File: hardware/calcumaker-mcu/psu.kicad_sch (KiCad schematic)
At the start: 21 parts, among them J1 USB-C, J2 BAT 1S Li-ion, Q1 AO3401A, U2 TPS63900DSKR, U3 USBLC6-2SC6, U4 MCP73831-2-OT

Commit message: hardware: 3-board split (MCU + keyboard + display), wired display, real connectors
Split the single logic board into three, wire the display as a KiCad
multi-channel design, and settle every interconnect on real, in-stock parts.

Three-board split (was two):
- Rename calcumaker-main -> calcumaker-mcu (brain/PSU logic board).
- New calcumaker-keyboard board: 50-key Cherry MX matrix + its own
  STM32G031K8U6 scanner (LCSC C432207, UFQFPN-32) + annunciator LEDs,
  mezzanine-stacked above the MCU board. Keyscanning is off the main board;
  only an I2C + UART link + KB_IRQ wake + power cross the mezzanine.

Display board (calcumaker-display):
- Corrected FJ5161AH to a SINGLE-digit 0.56" common-cathode part (C8093) --
  it is NOT a 4-digit module; 48 single digits (16/row x 3), authored symbol
  + 0.56" LTS6760 land. The old 4-digit CC56-12 mapping (and its 3D model)
  was the phantom "clock colon".
- Rebuilt as a KiCad multi-channel design: one reusable display_row.kicad_sch
  (1 TM1640 + 16 digits, fully wired) instantiated x3. Extended kschgen.py
  with wiring primitives + reused-sheet (multi-channel) support.

Connectors (real, verified LCSC / DigiKey parts):
- Display link -> 0.5mm 12P FFC: AFC01-S12FCA-00 (LCSC C262661) on both
  boards; cable = GCT FFC05-TIN 05-12-A-<len>-A-4-06-4-T (DigiKey accessory,
  length TBD). +5V/GND conductors doubled for the display LED current.
- Keyboard mezzanine -> low-profile Hirose DF40 (0.4mm, 2x5, 1.5mm stack):
  DF40C-10DS (C424636) + DF40C-10DP (C424635) -- dedicated KiCad footprint
  + 3D model, unlike the datasheet-less generic parts first considered.

Low-power & wake documented (two Stop domains; keypress -> G0 EXTI wake ->
KB_IRQ -> U575 WKUP; G0 also wakes on I2C address-match). calcumaker-core
is unchanged -- App still consumes (row,col).

All three boards generate + pass the structure check (mcu 52 / keyboard 119 /
display 60 components, all footprints assigned, no duplicate refs). Docs
(DESIGN.md, PARTS.md incl. a Non-B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
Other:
- title: Calcumaker 16 — Main — USB-C / Li-ion charge / load-share / buck-boost -> Calcumaker 16 — MCU — USB-C / Li-ion charge / load-share / buck-boost
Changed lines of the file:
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@@
 	(paper "A3")
 	(title_block
-		(title "Calcumaker 16 — Main — USB-C / Li-ion charge / load-share / buck-boost")
-		(date "2026-06-21")
-		(rev "0.1")
+		(title "Calcumaker 16 — MCU — USB-C / Li-ion charge / load-share / buck-boost")
+		(date "2026-07-05")
+		(rev "0.2")
 		(company "calcumaker authors")
 	)
@@
 		(pin "SH")
 		(instances
-			(project "calcumaker-main"
-				(path "/ca1c0000-0000-4000-8000-00000000ma01/b9ee67a8-aaed-4504-a49b-ae68f7f164a3"
+			(project "calcumaker-mcu"
+				(path "/ca1c0000-0000-4000-8000-00000000ma01/672f4fa7-1cc1-4703-8edf-f066cdb44902"
 					(reference "J1")
 					(unit 1)
@@
 		(pin "2")
 		(instances
-			(project "calcumaker-main"
-				(path "/ca1c0000-0000-4000-8000-00000000ma01/b9ee67a8-aaed-4504-a49b-ae68f7f164a3"
+			(project "calcumaker-mcu"
+				(path "/ca1c0000-0000-4000-8000-00000000ma01/672f4fa7-1cc1-4703-8edf-f066cdb44902"
 					(reference "J2")
 					(unit 1)
@@
 		(pin "11")
 		(instances
-			(project "calcumaker-main"
-				(path "/ca1c0000-0000-4000-8000-00000000ma01/b9ee67a8-aaed-4504-a49b-ae68f7f164a3"
+			(project "calcumaker-mcu"
+				(path "/ca1c0000-0000-4000-8000-00000000ma01/672f4fa7-1cc1-4703-8edf-f066cdb44902"
 					(reference "U2")
 					(unit 1)
@@
 		(pin "6")
 		(instances
-			(project "calcumaker-main"
-				(path "/ca1c0000-0000-4000-8000-00000000ma01/b9ee67a8-aaed-4504-a49b-ae68f7f164a3"
+			(project "calcumaker-mcu"
+				(path "/ca1c0000-0000-4000-8000-00000000ma01/672f4fa7-1cc1-4703-8edf-f066cdb44902"
 					(reference "U3")
 					(unit 1)
@@
 		(pin "2")
 		(instances
-			(project "calcumaker-main"
-				(path "/ca1c0000-0000-4000-8000-00000000ma01/b9ee67a8-aaed-4504-a49b-ae68f7f164a3"
+			(project "calcumaker-mcu"
+				(path "/ca1c0000-0000-4000-8000-00000000ma01/672f4fa7-1cc1-4703-8edf-f066cdb44902"
 					(reference "R1")
 					(unit 1)
@@
 		(pin "2")
 		(instances
-			(project "calcumaker-main"
-				(path "/ca1c0000-0000-4000-8000-00000000ma01/b9ee67a8-aaed-4504-a49b-ae68f7f164a3"
+			(project "calcumaker-mcu"
+				(path "/ca1c0000-0000-4000-8000-00000000ma01/672f4fa7-1cc1-4703-8edf-f066cdb44902"
 					(reference "R2")
 					(unit 1)
@@
 		(pin "5")
 		(instances
-			(project "calcumaker-main"
-				(path "/ca1c0000-0000-4000-8000-00000000ma01/b9ee67a8-aaed-4504-a49b-ae68f7f164a3"
+			(project "calcumaker-mcu"
+				(path "/ca1c0000-0000-4000-8000-00000000ma01/672f4fa7-1cc1-4703-8edf-f066cdb44902"
 					(reference "U4")
 					(unit 1)
@@
 		(pin "2")
 		(instances
-			(project "calcumaker-main"
-				(path "/ca1c0000-0000-4000-8000-00000000ma01/b9ee67a8-aaed-4504-a49b-ae68f7f164a3"
+			(project "calcumaker-mcu"
+				(path "/ca1c0000-0000-4000-8000-00000000ma01/672f4fa7-1cc1-4703-8edf-f066cdb44902"
 					(reference "R3")
 					(unit 1)
@@
 		(pin "2")
 		(instances
-			(project "calcumaker-main"
-				(path "/ca1c0000-0000-4000-8000-00000000ma01/b9ee67a8-aaed-4504-a49b-ae68f7f164a3"
+			(project "calcumaker-mcu"
+				(path "/ca1c0000-0000-4000-8000-00000000ma01/672f4fa7-1cc1-4703-8edf-f066cdb44902"
 					(reference "C1")
 					(unit 1)
@@
 		(pin "2")
 		(instances
-			(project "calcumaker-main"
-				(path "/ca1c0000-0000-4000-8000-00000000ma01/b9ee67a8-aaed-4504-a49b-ae68f7f164a3"
+			(project "calcumaker-mcu"
+				(path "/ca1c0000-0000-4000-8000-00000000ma01/672f4fa7-1cc1-4703-8edf-f066cdb44902"
 					(reference "C2")
 					(unit 1)
@@
 		(pin "3")
 		(instances
-			(project "calcumaker-main"
-				(path "/ca1c0000-0000-4000-8000-00000000ma01/b9ee67a8-aaed-4504-a49b-ae68f7f164a3"
+			(project "calcumaker-mcu"
+				(path "/ca1c0000-0000-4000-8000-00000000ma01/672f4fa7-1cc1-4703-8edf-f066cdb44902"
 					(reference "Q1")
 					(unit 1)
@@
 		(pin "2")
 		(instances
-			(project "calcumaker-main"
-				(path "/ca1c0000-0000-4000-8000-00000000ma01/b9ee67a8-aaed-4504-a49b-ae68f7f164a3"
+			(project "calcumaker-mcu"
+				(path "/ca1c0000-0000-4000-8000-00000000ma01/672f4fa7-1cc1-4703-8edf-f066cdb44902"
 					(reference "D1")
 					(unit 1)
@@
 		(pin "2")
 		(instances
-			(project "calcumaker-main"
-				(path "/ca1c0000-0000-4000-8000-00000000ma01/b9ee67a8-aaed-4504-a49b-ae68f7f164a3"
+			(project "calcumaker-mcu"
+				(path "/ca1c0000-0000-4000-8000-00000000ma01/672f4fa7-1cc1-4703-8edf-f066cdb44902"
 					(reference "R4")
 					(unit 1)
@@
 		(pin "2")
 		(instances
-			(project "calcumaker-main"
-				(path "/ca1c0000-0000-4000-8000-00000000ma01/b9ee67a8-aaed-4504-a49b-ae68f7f164a3"
+			(project "calcumaker-mcu"
+				(path "/ca1c0000-0000-4000-8000-00000000ma01/672f4fa7-1cc1-4703-8edf-f066cdb44902"
 					(reference "L1")
 					(unit 1)
@@
 		(pin "2")
 		(instances
-			(project "calcumaker-main"
-				(path "/ca1c0000-0000-4000-8000-00000000ma01/b9ee67a8-aaed-4504-a49b-ae68f7f164a3"
+			(project "calcumaker-mcu"
+				(path "/ca1c0000-0000-4000-8000-00000000ma01/672f4fa7-1cc1-4703-8edf-f066cdb44902"
 					(reference "C3")
 					(unit 1)
@@
 		(pin "2")
 		(instances
-			(project "calcumaker-main"
-				(path "/ca1c0000-0000-4000-8000-00000000ma01/b9ee67a8-aaed-4504-a49b-ae68f7f164a3"
+			(project "calcumaker-mcu"
+				(path "/ca1c0000-0000-4000-8000-00000000ma01/672f4fa7-1cc1-4703-8edf-f066cdb44902"
 					(reference "C4")
 					(unit 1)
@@
 		(pin "2")
 		(instances
-			(project "calcumaker-main"
-				(path "/ca1c0000-0000-4000-8000-00000000ma01/b9ee67a8-aaed-4504-a49b-ae68f7f164a3"
+			(project "calcumaker-mcu"
+				(path "/ca1c0000-0000-4000-8000-00000000ma01/672f4fa7-1cc1-4703-8edf-f066cdb44902"
 					(reference "C5")
 					(unit 1)
@@
 		(pin "2")
 		(instances
-			(project "calcumaker-main"
-				(path "/ca1c0000-0000-4000-8000-00000000ma01/b9ee67a8-aaed-4504-a49b-ae68f7f164a3"
+			(project "calcumaker-mcu"
+				(path "/ca1c0000-0000-4000-8000-00000000ma01/672f4fa7-1cc1-4703-8edf-f066cdb44902"
 					(reference "C6")
 					(unit 1)
@@
 		(pin "2")
 		(instances
-			(project "calcumaker-main"
-				(path "/ca1c0000-0000-4000-8000-00000000ma01/b9ee67a8-aaed-4504-a49b-ae68f7f164a3"
+			(project "calcumaker-mcu"
+				(path "/ca1c0000-0000-4000-8000-00000000ma01/672f4fa7-1cc1-4703-8edf-f066cdb44902"
 					(reference "C7")
 					(unit 1)
@@
 		(pin "2")
 		(instances
-			(project "calcumaker-main"
-				(path "/ca1c0000-0000-4000-8000-00000000ma01/b9ee67a8-aaed-4504-a49b-ae68f7f164a3"
+			(project "calcumaker-mcu"
+				(path "/ca1c0000-0000-4000-8000-00000000ma01/672f4fa7-1cc1-4703-8edf-f066cdb44902"
 					(reference "D2")
 					(unit 1)
@@
 		(pin "2")
 		(instances
-			(project "calcumaker-main"
-				(path "/ca1c0000-0000-4000-8000-00000000ma01/b9ee67a8-aaed-4504-a49b-ae68f7f164a3"
+			(project "calcumaker-mcu"
+				(path "/ca1c0000-0000-4000-8000-00000000ma01/672f4fa7-1cc1-4703-8edf-f066cdb44902"
 					(reference "R5")
 					(unit 1)

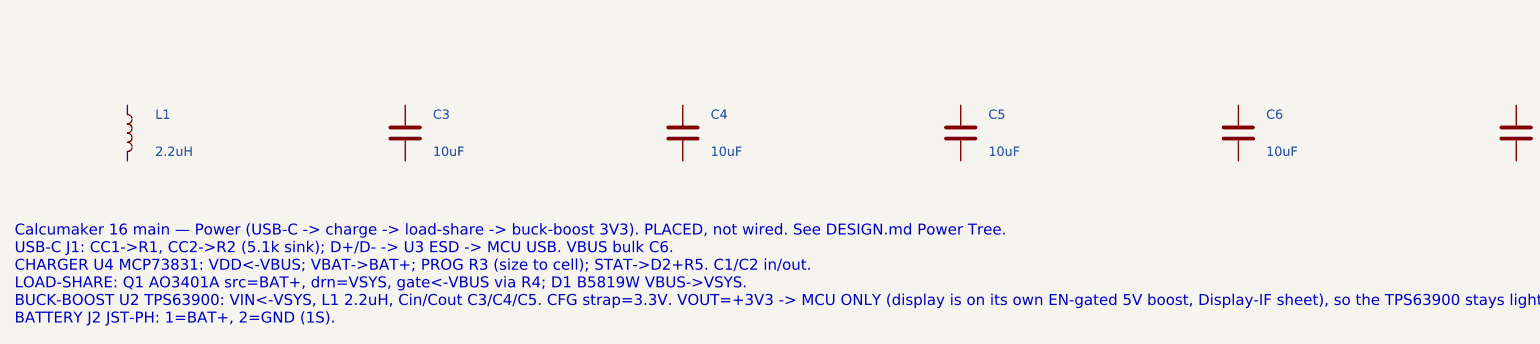
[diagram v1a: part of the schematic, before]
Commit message: docs: accuracy cleanup across README/DESIGN/PARTS + firmware/schgen comments
Sweep the docs and code comments to the three-board reality. Reviewed for
accuracy against the schematics/parts — no factual fixes were needed; this
also corrected several stale spots left over from the split:

- README / DESIGN.md / PARTS.md / reference: three-board split, 0.5mm FFC
  display link, Hirose DF40 mezzanine, STM32G0 keyboard scanner; drop stale
  "main board" phrasing; populate reference/README.md's datasheet table with
  the real parts (STM32G031K8U6, TM1640, FJ5161AH, AFC01-S12FCA-00 + GCT FFC,
  DF40C-10DS/DP).
- DESIGN.md Annunciators corrected to the keyboard board (D51-55 / R1-5,
  driven by the keyboard G0); Open Questions renumbered sequentially.
- firmware comments (keypad.rs / main.rs / Cargo.toml / README): keyboard-event
  intake over the mezzanine link + wake on KB_IRQ; fixed the wrong "host-tested
  with rug" note (it is the gmp-mpfr-nostd FFI). Comment-only, no logic change.
- schgen + .kicad_sch notes: "main" -> "MCU board", FFC/mezzanine references,
  TPS61022/MCU "no custom symbol".

All three boards still pass the structure check (mcu 52 / keyboard 119 /
display 60 components, no duplicate refs); the generator still compiles.

Co-Authored-By: Claude Opus 4.8 (1M context) <noreply@anthropic.com>
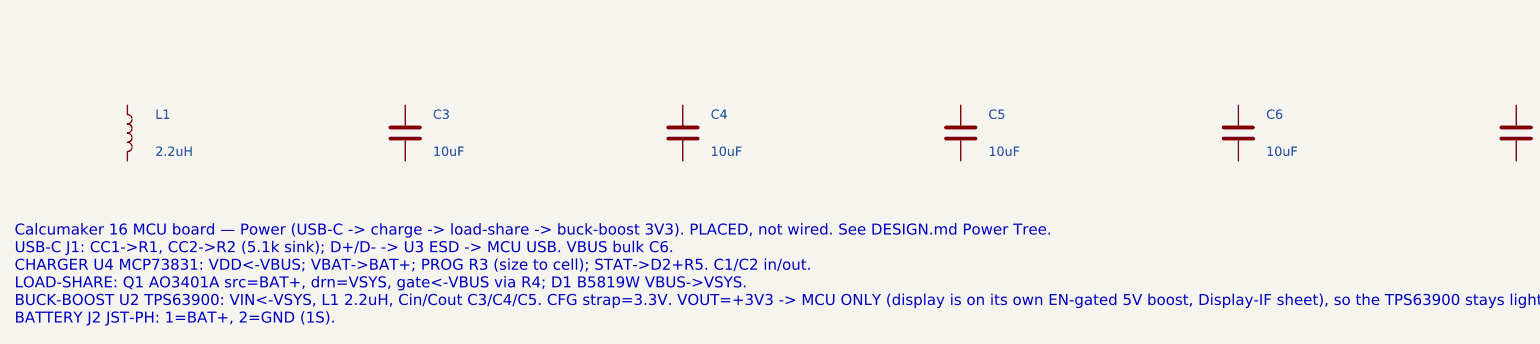
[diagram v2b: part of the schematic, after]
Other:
- note added: "Calcumaker 16 MCU board — Power (USB-C -> charge -> load-share -> buck-boost 3V3). PLACED, not wired. See DESIGN.md Power Tree. USB-C J1: CC1->R1, CC2->R2 (5.1k sink); D+/D- -> U3 ESD -> MCU USB. VBUS bulk C6. CHARGER U4 MCP73831: VDD<-VBUS; VBAT->BAT+; PROG R3 (size to cell); STAT->D2+R5. C1/C2 in/out. LOAD-SHARE: Q1 AO3401A src=BAT+, drn=VSYS, gate<-VBUS via R4; D1 B5819W VBUS->VSYS. BUCK-BOOST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"
- note removed: "Calcumaker 16 main — Power (USB-C -> charge -> load-share -> buck-boost 3V3). PLACED, not wired. See DESIGN.md Power Tree. USB-C J1: CC1->R1, CC2->R2 (5.1k sink); D+/D- -> U3 ESD -> MCU USB. VBUS bulk C6. CHARGER U4 MCP73831: VDD<-VBUS; VBAT->BAT+; PROG R3 (size to cell); STAT->D2+R5. C1/C2 in/out. LOAD-SHARE: Q1 AO3401A src=BAT+, drn=VSYS, gate<-VBUS via R4; D1 B5819W VBUS->VSYS. BUCK-BOOST U2 T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"
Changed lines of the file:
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@@
 		)
 	)
-	(text "Calcumaker 16 main — Power (USB-C -> charge -> load-share -> buck-boost 3V3). PLACED, not wired. See DESIGN.md Power Tree.\nUSB-C J1: CC1->R1, CC2->R2 (5.1k sink); D+/D- -> U3 ESD -> MCU USB. VBUS bulk C6.\nCHARGER U4 MCP73831: VDD<-VBUS; VBAT->BAT+; PROG R3 (size to cell); STAT->D2+R5. C1/C2 in/out.\nLOAD-SHARE: Q1 AO3401A src=BAT+, drn=VSYS, gate<-VBUS via R4; D1 B5819W VBUS->VSYS.\nBUCK-BOOST U2 TPS63900: VIN<-VSYS, L1 2.2uH, Cin/Cout C3/C4/C5. CFG strap=3.3V. VOUT=+3V3 -> MCU ONLY (display is on its own EN-gated 5V boost, Display-IF sheet), so the TPS63900 stays lightly loaded / low-Iq for sleep.\nBATTERY J2 JST-PH: 1=BAT+, 2=GND (1S)."
+	(text "Calcumaker 16 MCU board — Power (USB-C -> charge -> load-share -> buck-boost 3V3). PLACED, not wired. See DESIGN.md Power Tree.\nUSB-C J1: CC1->R1, CC2->R2 (5.1k sink); D+/D- -> U3 ESD -> MCU USB. VBUS bulk C6.\nCHARGER U4 MCP73831: VDD<-VBUS; VBAT->BAT+; PROG R3 (size to cell); STAT->D2+R5. C1/C2 in/out.\nLOAD-SHARE: Q1 AO3401A src=BAT+, drn=VSYS, gate<-VBUS via R4; D1 B5819W VBUS->VSYS.\nBUCK-BOOST U2 TPS63900: VIN<-VSYS, L1 2.2uH, Cin/Cout C3/C4/C5. CFG strap=3.3V. VOUT=+3V3 -> MCU ONLY (display is on its own EN-gated 5V boost, Display-IF sheet), so the TPS63900 stays lightly loaded / low-Iq for sleep.\nBATTERY J2 JST-PH: 1=BAT+, 2=GND (1S)."
 		(exclude_from_sim no)
 		(at 15.00 165.00 0)
